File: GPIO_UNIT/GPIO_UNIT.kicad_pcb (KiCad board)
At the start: 2 copper layers, 70 x 83.5 mm, 98 parts, among them J1001 Screw_Terminal_01x03, J1101 Screw_Terminal_01x03, J1201 Screw_Terminal_01x03, J1301 Conn_02x03_Odd_Even, J1401 Conn_02x03_Odd_Even, J401 Screw_Terminal_01x02, J501 Screw_Terminal_01x02, J601 Conn_02x03_Odd_Even, J701 USB_B_Mini, J702 Screw_Terminal_01x03, J801 Screw_Terminal_01x05, J901 Screw_Terminal_01x04, K1001 G6K-2F-Y-TR DC5, K1101 G6K-2F-Y-TR DC5, K1201 G6K-2F-Y-TR DC5, K701 G6K-2F-Y-TR DC5, Q1001 NPN_TOR, Q1101 NPN_TOR, Q1201 NPN_TOR, Q701 NPN_TOR, Q901 NPN_TOR, Q902 NPN_TOR, Q903 NPN_TOR, SW202 default_switch, SW801 SW_Push, SW802 SW_Push, SW803 SW_Push, SW804 SW_Push, U201 HEADER_3x2, U202 ATmega328-A, U301 L78L05_SOT89, U501 6N137, U701 CH340G, U801 24LC256, U901 MT2499A, Y201 Crystal_GND2, Y701 Crystal

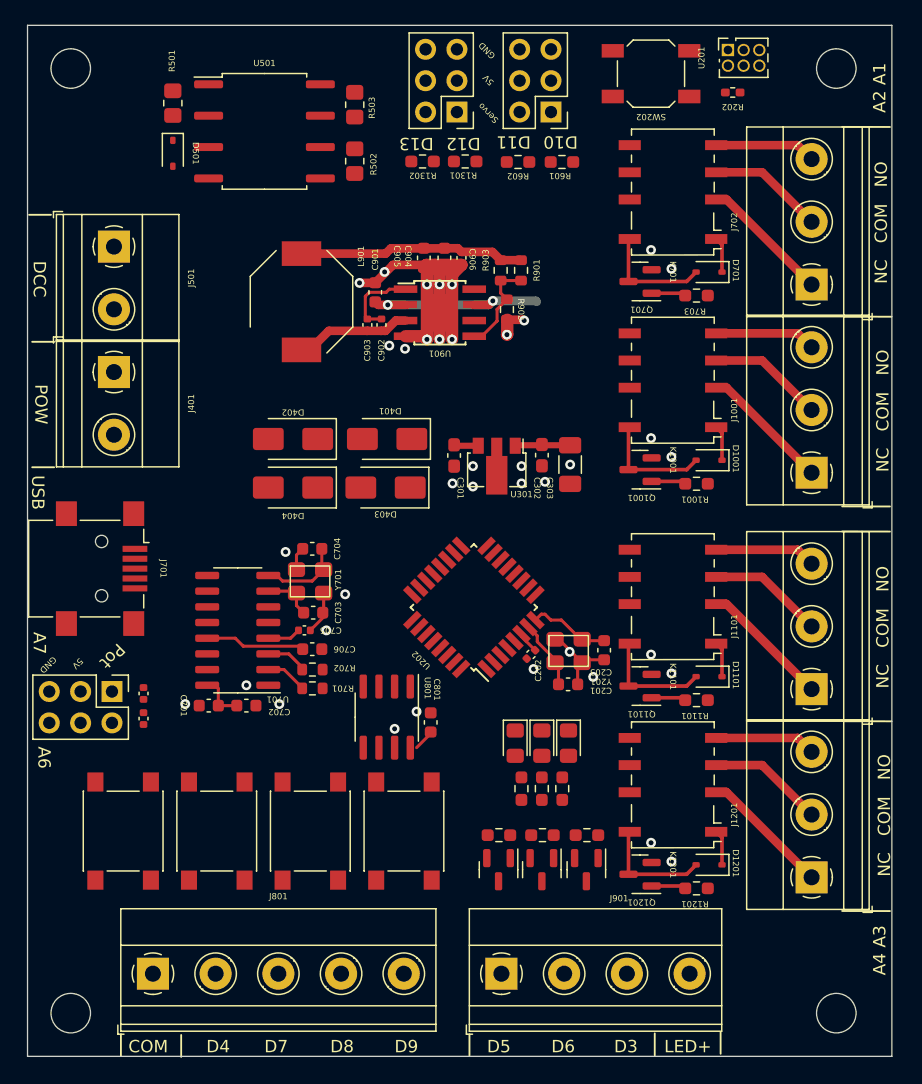
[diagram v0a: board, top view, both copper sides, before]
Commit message: Digital pins are now able to use the analog pinnumbering as well. Pin can be set to an analog or digital pin number by simply pressing a or d respectively when editting the pinnumbers. Take note that one can fill in invalid analog pinnumbers. Also due to me support the arduino mega, I should remove pin number limit all togather.
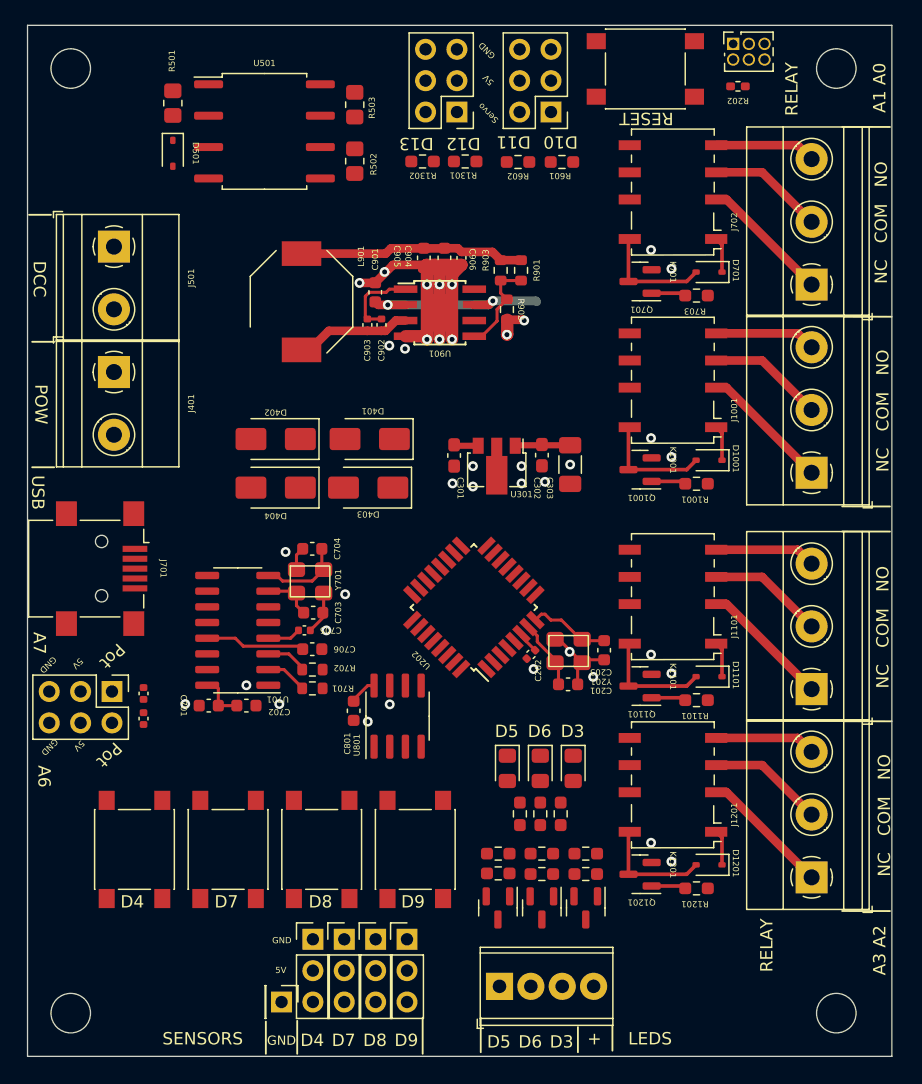
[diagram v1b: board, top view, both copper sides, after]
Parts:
- removed J801: Screw_Terminal_01x05, TerminalBlock_Phoenix:TerminalBlock_Phoenix_MKDS-1,5-5-5.08_1x05_P5.08mm_Horizontal
- added G***: LOGO, kicad_images:Train-Science logo, B.Cu at (191.6, 104.3)
- added J802: Conn_01x03_Pin, Connector_PinHeader_2.54mm:PinHeader_1x03_P2.54mm_Vertical, F.Cu at (197.2, 152.0)
- added J803: Conn_01x03_Pin, Connector_PinHeader_2.54mm:PinHeader_1x03_P2.54mm_Vertical, F.Cu at (194.7, 152.0)
- added J804: Conn_01x03_Pin, Connector_PinHeader_2.54mm:PinHeader_1x03_P2.54mm_Vertical, F.Cu at (192.2, 152.0)
- added J805: Conn_01x03_Pin, Connector_PinHeader_2.54mm:PinHeader_1x03_P2.54mm_Vertical, F.Cu at (189.6, 152.0)
- added J806: Conn_01x01_Pin, Connector_PinHeader_2.54mm:PinHeader_1x01_P2.54mm_Vertical, F.Cu at (187.1, 157.1)
- added R910: 22k, custom_kicad_lib_sk:R_0603_smalltext, F.Cu at (211.7, 145.1)
- added R911: 22k, custom_kicad_lib_sk:R_0603_smalltext, F.Cu at (208.2, 145.1)
- added R912: 22k, custom_kicad_lib_sk:R_0603_smalltext, F.Cu at (204.6, 145.1)
- added REF**: OSHW-Logo2_24.3x20mm_SilkScreen, Symbol:OSHW-Logo2_24.3x20mm_SilkScreen, B.Cu at (190.5, 130.7)
- J901: footprint TerminalBlock_Phoenix:TerminalBlock_Phoenix_MKDS-1,5-4-5.08_1x04_P5.08mm_Horizontal -> TerminalBlock_Phoenix:TerminalBlock_Phoenix_MPT-0,5-4-2.54_1x04_P2.54mm_Horizontal
- Q901, Q902, Q903: value NPN_TOR -> AO3400A
- R904, R905, R906: value 1k -> 22R
- SW202: value default_switch -> SW_Push; footprint custom_kicad_lib_sk:default_switch -> custom_kicad_lib_sk:tactile_SMD_6mm
- moved C801 6.31 mm to (192.9, 133.5), turned to 90 degrees
- moved R904 3.15 mm to (211.7, 146.7)
- moved R905 3.15 mm to (208.2, 146.7)
- moved R906 3.10 mm to (204.6, 146.7)
- moved Q903 3.10 mm to (204.6, 149.5)
- moved Q901 3.10 mm to (211.7, 149.5)
- moved Q902 3.10 mm to (208.2, 149.5)
- moved D903 2.14 mm to (205.4, 138.2)
- moved D901 2.08 mm to (210.7, 138.2)
- moved R907 2.04 mm to (209.7, 141.9)
- moved R909 2.04 mm to (206.4, 141.9)
- moved D902 2.04 mm to (208.0, 138.2)
- moved R908 2.04 mm to (208.0, 141.9)
- moved SW802 1.75 mm to (190.3, 144.7)
- moved SW804 1.75 mm to (175.2, 144.7)
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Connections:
- Q901 pad 1: Net-(Q901-B) -> Net-(Q901-G)
- Q902 pad 1: Net-(Q902-B) -> Net-(Q902-G)
- Q903 pad 1: Net-(Q903-B) -> Net-(Q903-G)
- R904 pad 1: Net-(Q901-B) -> /L1
- R904 pad 2: /L1 -> Net-(Q901-G)
- R905 pad 1: Net-(Q902-B) -> /L2
- R905 pad 2: /L2 -> Net-(Q902-G)
- R906 pad 1: Net-(Q903-B) -> /L3
- R906 pad 2: /L3 -> Net-(Q903-G)
- U202 pad 27: /CPU/A4 -> /SDA
- U202 pad 28: /CPU/A5 -> /SCL
- U801 pad 5: /eeprom/SDA -> /SDA
- U801 pad 6: /eeprom/SCL -> /SCL
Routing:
- net +5V: track 11.7 -> 12.3 mm
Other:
- board text added: "+"
- board text added: "3 options - CS add-on - Screw terminal for switches - 4x3P connectors for IR sluices or LDS boards."
- board text added: "A1 A0"
- board text added: "A3 A2"
- board text added: "Default progams: FunctionBlox - AHOB (w DCC as extra) DONE - servo / relay / led decoder (!DCC EXT!! for brightness) and switches - servo with frog relay decoder + led. and switches - pot control for servo's and led brightness and switches - turning loop unit base on current sense Code - Single analog weistra controller with pots/DCC with shuttle option and CS (4 buttons left for servo's or the r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"
- board text added: "LEDS"
- board text added: "NOTE - DCC can be used as power - with the CS, pots, relays and PWM channels, one can do 2 analog trains and shuttle."
- board text added: "RELAY"
- board text added: "RESET"
- board text added: "SENSORS"
- board text added: "Suplementing stuff - CS board + 0 degree 5P header - Servo motors - Potentiometer boards - IR light sluices (not assembled) + headers 2x 2x3 header - red LEDs with 1K5 resistors - screw terminals - Shunt resistors for analog - 1A PSUs"
- board text added: "Train-Science Development Board Jack Of all Trades"
- board text removed: "A2 A1"
- board text removed: "A4 A3"
- board text removed: "COM"
- board text removed: "LED+"
